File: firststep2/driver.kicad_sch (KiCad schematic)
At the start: 9 parts

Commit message: firststep2
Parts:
- removed SW?: RELAY_SW, symbol Switch:SW_SPST
- added J10: Arduino_D6, symbol Connector:Conn_01x01_Male
- added J11: RELAY_SW, symbol Connector:Conn_01x02_Male
- added J12: RELAY_PWR, symbol Connector:Conn_01x02_Male
- added J13: Arduino_D9, symbol Connector:Conn_01x01_Male
- added J9: Conn_MOTOR, symbol Connector:Conn_01x01_Male
- added Q1: Q_NMOS_DGS, symbol Device:Q_NMOS_DGS
- C7: renamed from C?; value 3,3u -> (none); footprint Capacitor_THT:C_Disc_D3.0mm_W2.0mm_P2.50mm -> (none)
- R13, R14: renamed from R?; value 3,3 -> (none); footprint Resistor_THT:R_Axial_DIN0204_L3.6mm_D1.6mm_P7.62mm_Horizontal -> (none)
- U4: renamed from U?; value MIC4428 -> (none); footprint Package_DIP:DIP-8_W7.62mm_Socket -> (none)
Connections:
- net GND: now also J12.1 (Pin_1), Q1.3 (S)
- net PB1: now also J13.1 (Pin_1)
- net PD6: now also J10.1 (Pin_1)
- net +12V renamed VCC
- net VCC: now also J11.1 (Pin_1)
- net FET_GATE: no longer names the net of R13.2
- net FET_GATE: now also Q1.2 (G)
- net RELAY_CTRL: no longer names the net of R2.1, R2.2
- net RELAY_CTRL: now also J11.2 (Pin_2), J12.2 (Pin_2)
- new net: J9.1 (Pin_1), Q1.1 (D)

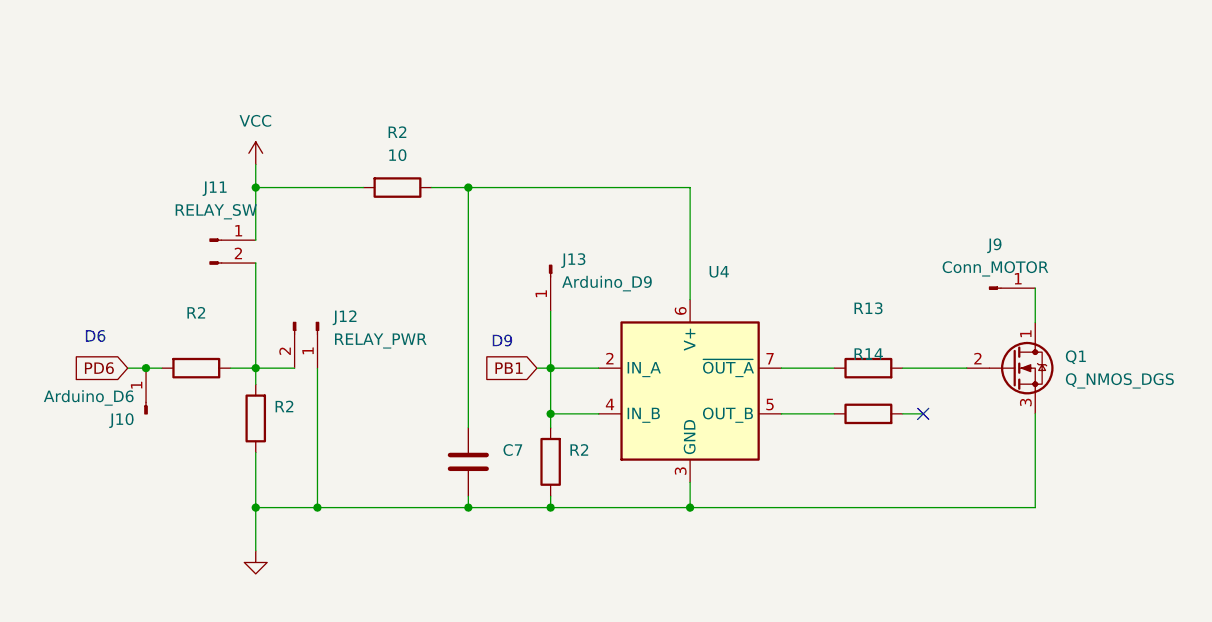
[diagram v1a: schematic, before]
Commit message: added atmega_logic, changed lm to tl
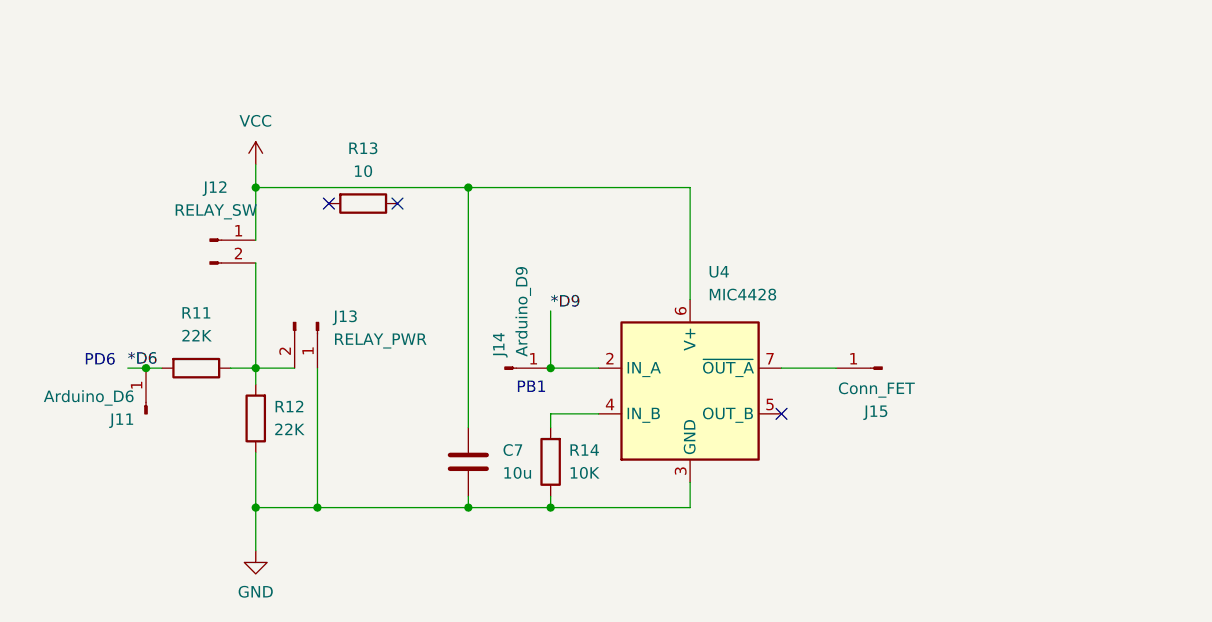
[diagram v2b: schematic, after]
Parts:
- removed Q1: Q_NMOS_DGS, symbol Device:Q_NMOS_DGS
- removed R13, R14: (no value), symbol Device:R
- C7: value (none) -> 10u; footprint (none) -> Capacitor_THT:C_Radial_D5.0mm_H5.0mm_P2.00mm
- J11: renamed from J10; footprint (none) -> Connector_PinHeader_2.54mm:PinHeader_1x01_P2.54mm_Vertical
- J12: renamed from J11; footprint (none) -> Connector_PinHeader_2.54mm:PinHeader_1x02_P2.54mm_Vertical
- J13: renamed from J12; footprint (none) -> Connector_PinHeader_2.54mm:PinHeader_1x01_P2.54mm_Vertical
- J14: renamed from J13; footprint (none) -> Connector_PinHeader_2.54mm:PinHeader_1x01_P2.54mm_Vertical
- J15: renamed from J9; value Conn_MOTOR -> Conn_FET; footprint (none) -> Connector_PinHeader_2.54mm:PinHeader_1x01_P2.54mm_Vertical
- R11, R12: renamed from R2; value 330 -> 22K; footprint R_Axial_DIN0207_L6.3mm_D2.5mm_P7.62mm_Horizontal -> Resistor_THT:R_Axial_DIN0207_L6.3mm_D2.5mm_P7.62mm_Horizontal
- R13: renamed from R2; value 330 -> 10; footprint R_Axial_DIN0207_L6.3mm_D2.5mm_P7.62mm_Horizontal -> Resistor_THT:R_Axial_DIN0411_L9.9mm_D3.6mm_P12.70mm_Horizontal
- R14: renamed from R2; value 330 -> 10K; footprint R_Axial_DIN0207_L6.3mm_D2.5mm_P7.62mm_Horizontal -> Resistor_THT:R_Axial_DIN0207_L6.3mm_D2.5mm_P7.62mm_Horizontal
- U4: value (none) -> MIC4428; footprint (none) -> Package_DIP:DIP-8_W7.62mm_Socket
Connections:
- net VCC: now also C7.1, U4.6 (V+); no longer R13.2
- net at U4.7 (~{OUT_A}): now also J15.1 (Pin_1)
- net PB1: no longer names the net of R14.2, U4.4 (IN_B)
- net PB1: no longer J14.1 (Pin_1), U4.2 (IN_A)
- net PD6 renamed *D6
- new net *D9: J14.1 (Pin_1), U4.2 (IN_A)
- now unconnected: R13.1
- no-connect marks 1 -> 3
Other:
- note added: "PB1"
- note added: "PD6"
- note removed: "D6"
- note removed: "D9"
- moved on the sheet: J14, J15, R13

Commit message: update pcb
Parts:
- renumbered R12 to R10, R13 to R11, R14 to R12, R11 to R9
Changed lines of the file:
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@@
   (symbol (lib_id "Device:R") (at 76.962 50.038 270) (unit 1)
     (in_bom yes) (on_board yes) (fields_autoplaced)
-    (property "Reference" "R13" (id 0) (at 76.962 43.942 90))
+    (property "Reference" "R11" (id 0) (at 76.962 43.942 90))
     (property "Value" "10" (id 1) (at 76.962 46.482 90))
     (property "Footprint" "Resistor_THT:R_Axial_DIN0411_L9.9mm_D3.6mm_P12.70mm_Horizontal" (id 2) (at 76.962 48.26 90)
@@
   (symbol (lib_id "Device:R") (at 97.79 78.74 180) (unit 1)
     (in_bom yes) (on_board yes) (fields_autoplaced)
-    (property "Reference" "R14" (id 0) (at 99.822 77.4699 0)
+    (property "Reference" "R12" (id 0) (at 99.822 77.4699 0)
       (effects (font (size 1.27 1.27)) (justify right))
     )
@@
   (symbol (lib_id "Device:R") (at 65.024 73.914 180) (unit 1)
     (in_bom yes) (on_board yes) (fields_autoplaced)
-    (property "Reference" "R12" (id 0) (at 67.056 72.6439 0)
+    (property "Reference" "R10" (id 0) (at 67.056 72.6439 0)
       (effects (font (size 1.27 1.27)) (justify right))
     )
@@
   (symbol (lib_id "Device:R") (at 58.42 68.326 270) (unit 1)
     (in_bom yes) (on_board yes) (fields_autoplaced)
-    (property "Reference" "R11" (id 0) (at 58.42 62.23 90))
+    (property "Reference" "R9" (id 0) (at 58.42 62.23 90))
     (property "Value" "22K" (id 1) (at 58.42 64.77 90))
     (property "Footprint" "Resistor_THT:R_Axial_DIN0207_L6.3mm_D2.5mm_P7.62mm_Horizontal" (id 2) (at 58.42 66.548 90)

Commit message: update pcb
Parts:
- J13: footprint Connector_PinHeader_2.54mm:PinHeader_1x01_P2.54mm_Vertical -> Connector_PinHeader_2.54mm:PinHeader_1x02_P2.54mm_Vertical
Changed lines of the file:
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@@
       (effects (font (size 1.27 1.27)) (justify left))
     )
-    (property "Footprint" "Connector_PinHeader_2.54mm:PinHeader_1x01_P2.54mm_Vertical" (id 2) (at 71.882 63.246 0)
+    (property "Footprint" "Connector_PinHeader_2.54mm:PinHeader_1x02_P2.54mm_Vertical" (id 2) (at 71.882 63.246 0)
       (effects (font (size 1.27 1.27)) hide)
     )
